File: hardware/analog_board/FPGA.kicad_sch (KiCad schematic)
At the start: 0 parts

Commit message: 1、FPGA最小系统原理图 2、DAC电路原理图 3、FPGA DAC 预布局
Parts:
- added R21: 100R, Resistor_SMD:R_0402_1005Metric, symbol Device:R
- added RN2, RN3, RN4, RN5, RN6, RN7, RN8, RN9: 33R, Resistor_SMD:R_Array_Concave_4x0402, symbol Device:R_Pack04
- added U1: GW2A-LV18EQ144, ArbWave30_lib:QFP-144_20x20_Pitch0.5mm, symbol ArbWave30_lib:GW2AR-LV18EQ144C8/I7
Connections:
- new net: RN7.5 (R4.2), U1.64 (IOB40A)
- new net: RN7.6 (R3.2), U1.63 (IOB38B)
- new net: RN7.7 (R2.2), U1.62 (IOB38A)
- new net: RN7.8 (R1.2), U1.61 (IOB34B)
- new net: RN3.5 (R4.2), U1.49 (IOB17B)
- new net: RN3.6 (R3.2), U1.48 (IOB17A)
- new net: RN3.7 (R2.2), U1.47 (IOB14B)
- new net: RN3.8 (R1.2), U1.46 (IOB14A)
- new net: RN2.5 (R4.2), U1.54 (IOB22B)
- new net: RN2.6 (R3.2), U1.52 (IOB22A)
- new net: RN2.7 (R2.2), U1.51 (IOB20B)
- new net: RN2.8 (R1.2), U1.50 (IOB20A)
- new net: RN9.5 (R4.2), U1.72 (IOB55B)
- new net: RN9.6 (R3.2), U1.71 (IOB53B)
- new net: RN9.7 (R2.2), U1.70 (IOB53A)
- new net: RN9.8 (R1.2), U1.69 (IOB48B)
- new net: RN5.8 (R1.2), U1.38 (IOB5A)
- new net: RN5.7 (R2.2), U1.39 (IOB5B)
- new net: RN5.6 (R3.2), U1.40 (IOB6A)
- new net: RN5.5 (R4.2), U1.41 (IOB6B)
- new net: RN4.8 (R1.2), U1.42 (IOB7A)
- new net: RN4.7 (R2.2), U1.43 (IOB7B)
- new net: RN4.6 (R3.2), U1.44 (IOB12A)
- new net: RN4.5 (R4.2), U1.45 (IOB12B)
- new net: RN8.5 (R4.2), U1.68 (IOB48A)
- new net: RN8.6 (R3.2), U1.67 (IOB42B)
- new net: RN8.7 (R2.2), U1.66 (IOB42A)
- new net: RN8.8 (R1.2), U1.65 (IOB40B)
- new net: RN6.8 (R1.2), U1.57 (IOB30B/GCLKC_4)
- new net: RN6.7 (R2.2), U1.58 (IOB33A)
- new net: RN6.6 (R3.2), U1.59 (IOB33B)
- new net: RN6.5 (R4.2), U1.60 (IOB34A)
- new net +3.3V: U1.103 (VCCX/VCC_IO2/VCC_IO6/VCC_IO7), U1.109 (VCC_IO1), U1.127 (VCC_IO0), U1.19 (VCCX/VCC_IO2/VCC_IO6/VCC_IO7), U1.31 (VCCX/VCC_IO2/VCC_IO6/VCC_IO7), U1.37 (VCC_IO5), U1.5 (VCCX/VCC_IO2/VCC_IO6/VCC_IO7), U1.55 (VCC_IO4), U1.77 (VCC_IO3), U1.91 (VCC_IO3)
- new net Ctrl_FPGA_NRST: U1.128 (IOT19A)
- new net Ctrl_SPI_CLK: U1.131 (IOT14B)
- new net Ctrl_SPI_CS: U1.132 (IOT14A)
- new net Ctrl_SPI_MISO: U1.130 (IOT17A)
- new net Ctrl_SPI_MOSI: U1.129 (IOT17B)
- new net DAC_SPI.DAC_SPI_CLK: U1.33 (IOL42B)
- new net DAC_SPI.DAC_SPI_CS: U1.32 (IOL42A)
- new net DAC_SPI.DAC_SPI_MISO: U1.35 (IOL45B/LPLL2_C_in)
- new net DAC_SPI.DAC_SPI_MOSI: U1.34 (IOL45A/LPLL2_T_in)
- new net Data_Clock: U1.56 (IOB30A/GCLKT_4)
- new net FPGA_CLK+: R21.2, U1.106 (IOR7A/RPLL1_T_in)
- new net FPGA_CLK-: R21.1, U1.105 (IOR7B/RPLL1_C_in)
- new net GND: U1.107 (VSS), U1.145 (EPAD), U1.17 (VSS), U1.2 (VSS), U1.53 (VSS), U1.74 (VSS), U1.89 (VSS)
- new net P1D0: RN6.1 (R1.1)
- new net P1D1: RN6.2 (R2.1)
- new net P1D10: RN8.3 (R3.1)
- new net P1D11: RN8.4 (R4.1)
- new net P1D12: RN9.1 (R1.1)
- new net P1D13: RN9.2 (R2.1)
- new net P1D14: RN9.3 (R3.1)
- new net P1D15: RN9.4 (R4.1)
- new net P1D2: RN6.3 (R3.1)
- new net P1D3: RN6.4 (R4.1)
- new net P1D4: RN7.1 (R1.1)
- new net P1D5: RN7.2 (R2.1)
- new net P1D6: RN7.3 (R3.1)
- new net P1D7: RN7.4 (R4.1)
- new net P1D8: RN8.1 (R1.1)
- new net P1D9: RN8.2 (R2.1)
- new net P2D0: RN5.1 (R1.1)
- new net P2D1: RN5.2 (R2.1)
- new net P2D10: RN3.3 (R3.1)
- new net P2D11: RN3.4 (R4.1)
- new net P2D12: RN2.1 (R1.1)
- new net P2D13: RN2.2 (R2.1)
- new net P2D14: RN2.3 (R3.1)
- new net P2D15: RN2.4 (R4.1)
- new net P2D2: RN5.3 (R3.1)
- new net P2D3: RN5.4 (R4.1)
- new net P2D4: RN4.1 (R1.1)
- new net P2D5: RN4.2 (R2.1)
- new net P2D6: RN4.3 (R3.1)
- new net P2D7: RN4.4 (R4.1)
- new net P2D8: RN3.1 (R1.1)
- new net P2D9: RN3.2 (R2.1)
- new net VCC_Core: U1.1 (VCC/VCC_PLLL1), U1.108 (VCC/VCC_PLLL1), U1.36 (VCC/VCC_PLLL1), U1.73 (VCC/VCC_PLLL1)
- new net VCC_PLLL: U1.8 (VCCPLL_L0)
- new net VCC_PLLR: U1.104 (VCCPLL_R0), U1.81 (VCCPLL_R1)

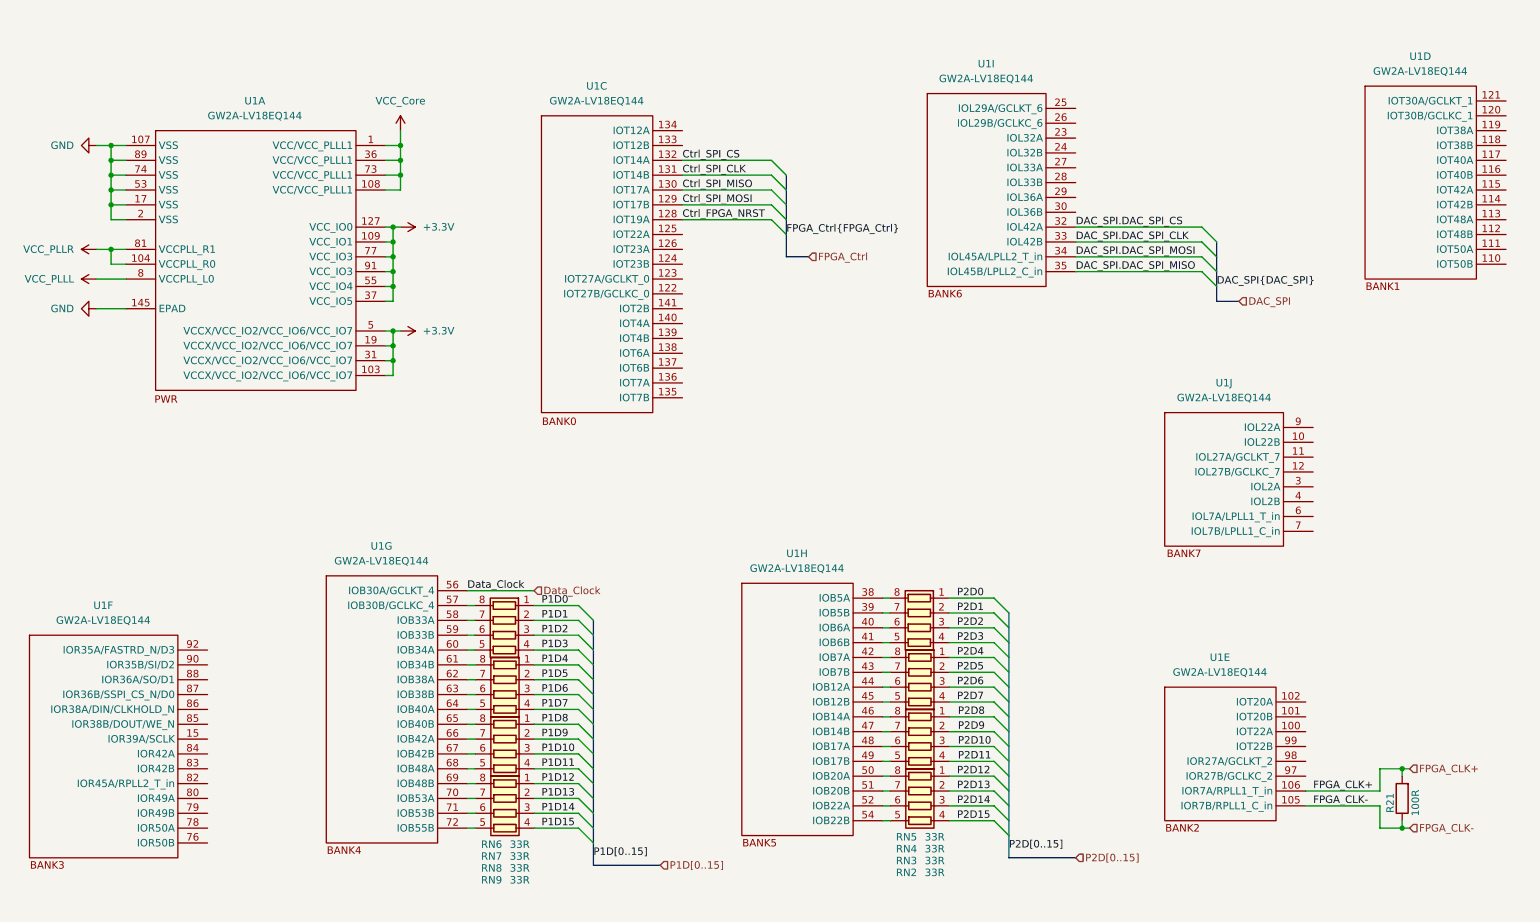
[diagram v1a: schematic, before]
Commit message: feat: 滤波器&差分转单端电路原理图
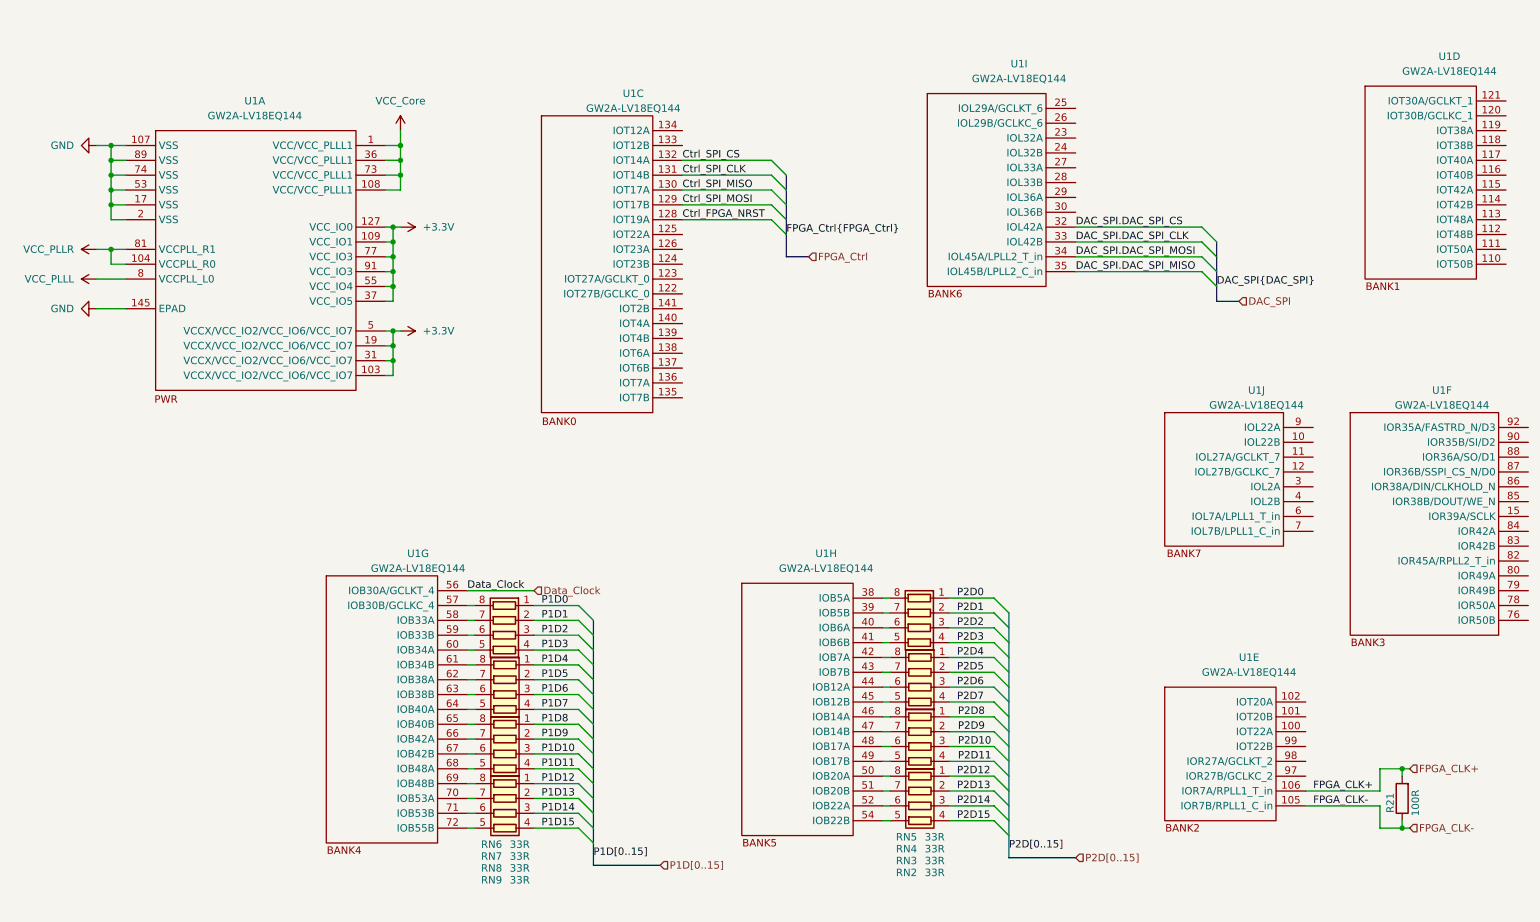
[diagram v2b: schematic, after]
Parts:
- U1: footprint ArbWave30_lib:QFP-144_20x20_Pitch0.5mm -> ArbWave30_lib:LQFP-144_20x20_Pitch0.5mm
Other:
- moved on the sheet: U1F
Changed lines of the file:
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@@
 		)
 	)
+	(rule_area
+		(exclude_from_sim no)
+		(in_bom yes)
+		(on_board yes)
+		(dnp no)
+		(polyline
+			(pts
+				(xy 172.085 110.49) (xy 172.72 157.48) (xy 189.23 157.48) (xy 188.595 110.49)
+			)
+			(stroke
+				(width 0)
+				(type dash)
+			)
+			(fill
+				(type none)
+			)
+		)
+	)
+	(rule_area
+		(exclude_from_sim no)
+		(in_bom yes)
+		(on_board yes)
+		(dnp no)
+		(polyline
+			(pts
+				(xy 100.965 109.22) (xy 101.6 156.21) (xy 118.11 156.21) (xy 117.475 109.22)
+			)
+			(stroke
+				(width 0)
+				(type dash)
+			)
+			(fill
+				(type none)
+			)
+		)
+	)
+	(netclass_flag ""
+		(length 2.54)
+		(shape round)
+		(at 104.14 109.22 0)
+		(fields_autoplaced yes)
+		(effects
+			(font
+				(size 1.27 1.27)
+			)
+			(justify left bottom)
+		)
+		(property "网络类" "DAC_data_port"
+			(at 104.8385 106.68 0)
+			(show_name no)
+			(do_not_autoplace no)
+			(effects
+				(font
+					(size 1.27 1.27)
+				)
+				(justify left)
+			)
+		)
+		(property "Component Class" ""
+			(at -39.37 -8.89 0)
+			(show_name no)
+			(do_not_autoplace no)
+			(effects
+				(font
+					(size 1.27 1.27)
+					(italic yes)
+				)
+			)
+		)
+	)
+	(netclass_flag ""
+		(length 2.54)
+		(shape round)
+		(at 175.26 110.49 0)
+		(fields_autoplaced yes)
+		(effects
+			(font
+				(size 1.27 1.27)
+			)
+			(justify left bottom)
+		)
+		(property "网络类" "DAC_data_port"
+			(at 175.9585 107.95 0)
+			(show_name no)
+			(do_not_autoplace no)
+			(effects
+				(font
+					(size 1.27 1.27)
+				)
+				(justify left)
+			)
+		)
+		(property "Component Class" ""
+			(at 31.75 -7.62 0)
+			(show_name no)
+			(do_not_autoplace no)
+			(effects
+				(font
+					(size 1.27 1.27)
+					(italic yes)
+				)
+			)
+		)
+	)
 	(symbol
 		(lib_id "Device:R")
@@
 		(fields_autoplaced yes)
 		(property "Reference" "U1"
-			(at 230.4312 124.46 0)
+			(at 235.4205 124.46 0)
 			(show_name no)
 			(do_not_autoplace no)
@@
 		)
 		(property "Value" "GW2A-LV18EQ144"
-			(at 230.4312 127 0)
+			(at 235.4205 127 0)
 			(show_name no)
 			(do_not_autoplace no)
@@
 			)
 		)
-		(property "Footprint" "ArbWave30_lib:QFP-144_20x20_Pitch0.5mm"
+		(property "Footprint" "ArbWave30_lib:LQFP-144_20x20_Pitch0.5mm"
 			(at 229.616 122.682 0)
 			(hide yes)
@@
 		(fields_autoplaced yes)
 		(property "Reference" "U1"
-			(at 264.7212 21.59 0)
+			(at 269.7105 21.59 0)
 			(show_name no)
 			(do_not_autoplace no)
@@
 		)
 		(property "Value" "GW2A-LV18EQ144"
-			(at 264.7212 24.13 0)
+			(at 269.7105 24.13 0)
 			(show_name no)
 			(do_not_autoplace no)
@@
 			)
 		)
-		(property "Footprint" "ArbWave30_lib:QFP-144_20x20_Pitch0.5mm"
+		(property "Footprint" "ArbWave30_lib:LQFP-144_20x20_Pitch0.5mm"
 			(at 263.906 19.812 0)
 			(hide yes)
@@
 		(fields_autoplaced yes)
 		(property "Reference" "U1"
-			(at 158.0412 106.68 0)
+			(at 163.0305 106.68 0)
 			(show_name no)
 			(do_not_autoplace no)
@@
 		)
 		(property "Value" "GW2A-LV18EQ144"
-			(at 158.0412 109.22 0)
+			(at 163.0305 109.22 0)
 			(show_name no)
 			(do_not_autoplace no)
@@
 			)
 		)
-		(property "Footprint" "ArbWave30_lib:QFP-144_20x20_Pitch0.5mm"
+		(property "Footprint" "ArbWave30_lib:LQFP-144_20x20_Pitch0.5mm"
 			(at 157.226 104.902 0)
 			(hide yes)
@@
 	(symbol
 		(lib_id "ArbWave30_lib:GW2AR-LV18EQ144C8/I7")
-		(at 24.13 118.11 0)
+		(at 250.19 80.01 0)
 		(unit 6)
 		(body_style 1)
@@
 		(fields_autoplaced yes)
 		(property "Reference" "U1"
-			(at 39.2962 115.57 0)
+			(at 268.4405 78.74 0)
 			(show_name no)
 			(do_not_autoplace no)
@@
 		)
 		(property "Value" "GW2A-LV18EQ144"
-			(at 39.2962 118.11 0)
+			(at 268.4405 81.28 0)
 			(show_name no)
 			(do_not_autoplace no)
@@
 			)
 		)
-		(property "Footprint" "ArbWave30_lib:QFP-144_20x20_Pitch0.5mm"
-			(at 36.576 115.062 0)
+		(property "Footprint" "ArbWave30_lib:LQFP-144_20x20_Pitch0.5mm"
+			(at 262.636 76.962 0)
 			(hide yes)
 			(show_name no)
@@
 		)
 		(property "Datasheet" ""
-			(at 24.13 118.11 0)
+			(at 250.19 80.01 0)
 			(hide yes)
 			(show_name no)
@@
 		)
 		(property "Description" ""
-			(at 24.13 118.11 0)
+			(at 250.19 80.01 0)
 			(hide yes)
 			(show_name no)
@@
 		(fields_autoplaced yes)
 		(property "Reference" "U1"
-			(at 86.9212 105.41 0)
+			(at 93.1805 106.68 0)
 			(show_name no)
 			(do_not_autoplace no)
@@
 		)
 		(property "Value" "GW2A-LV18EQ144"
-			(at 86.9212 107.95 0)
+			(at 93.1805 109.22 0)
 			(show_name no)
 			(do_not_autoplace no)
@@
 			)
 		)
-		(property "Footprint" "ArbWave30_lib:QFP-144_20x20_Pitch0.5mm"
+		(property "Footprint" "ArbWave30_lib:LQFP-144_20x20_Pitch0.5mm"
 			(at 87.376 104.902 0)
 			(hide yes)
@@
 		(fields_autoplaced yes)
 		(property "Reference" "U1"
-			(at 123.7512 26.67 0)
+			(at 130.0105 27.94 0)
 			(show_name no)
 			(do_not_autoplace no)
@@
 		)
 		(property "Value" "GW2A-LV18EQ144"
-			(at 123.7512 29.21 0)
+			(at 130.0105 30.48 0)
 			(show_name no)
 			(do_not_autoplace no)
@@
 			)
 		)
-		(property "Footprint" "ArbWave30_lib:QFP-144_20x20_Pitch0.5mm"
+		(property "Footprint" "ArbWave30_lib:LQFP-144_20x20_Pitch0.5mm"
 			(at 124.206 26.162 0)
 			(hide yes)
@@
 		(fields_autoplaced yes)
 		(property "Reference" "U1"
-			(at 190.4262 22.86 0)
+			(at 196.0505 22.86 0)
 			(show_name no)
 			(do_not_autoplace no)
@@
 		)
 		(property "Value" "GW2A-LV18EQ144"
-			(at 190.4262 25.4 0)
+			(at 196.0505 25.4 0)
 			(show_name no)
 			(do_not_autoplace no)
@@
 			)
 		)
-		(property "Footprint" "ArbWave30_lib:QFP-144_20x20_Pitch0.5mm"
+		(property "Footprint" "ArbWave30_lib:LQFP-144_20x20_Pitch0.5mm"
 			(at 190.246 21.082 0)
 			(hide yes)
@@
 		(fields_autoplaced yes)
 		(property "Reference" "U1"
-			(at 231.14 77.47 0)
+			(at 236.6905 78.74 0)
 			(show_name no)
 			(do_not_autoplace no)
@@
 		)
 		(property "Value" "GW2A-LV18EQ144"
-			(at 231.14 80.01 0)
+			(at 236.6905 81.28 0)
 			(show_name no)
 			(do_not_autoplace no)
@@
 			)
 		)
-		(property "Footprint" "ArbWave30_lib:QFP-144_20x20_Pitch0.5mm"
+		(property "Footprint" "ArbWave30_lib:LQFP-144_20x20_Pitch0.5mm"
 			(at 230.886 76.962 0)
 			(hide yes)
@@
 			)
 		)
-		(property "Footprint" "ArbWave30_lib:QFP-144_20x20_Pitch0.5mm"
+		(property "Footprint" "ArbWave30_lib:LQFP-144_20x20_Pitch0.5mm"
 			(at 59.436 27.432 0)
 			(hide yes)

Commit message: feat：时钟电路原理图
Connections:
- net Clock_NRST: now reaches U1.110 (IOT50B)
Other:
- moved on the sheet: R21, RN2, RN3, RN4, RN5, RN6, RN7, RN8, RN9, U1D, U1E, U1F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

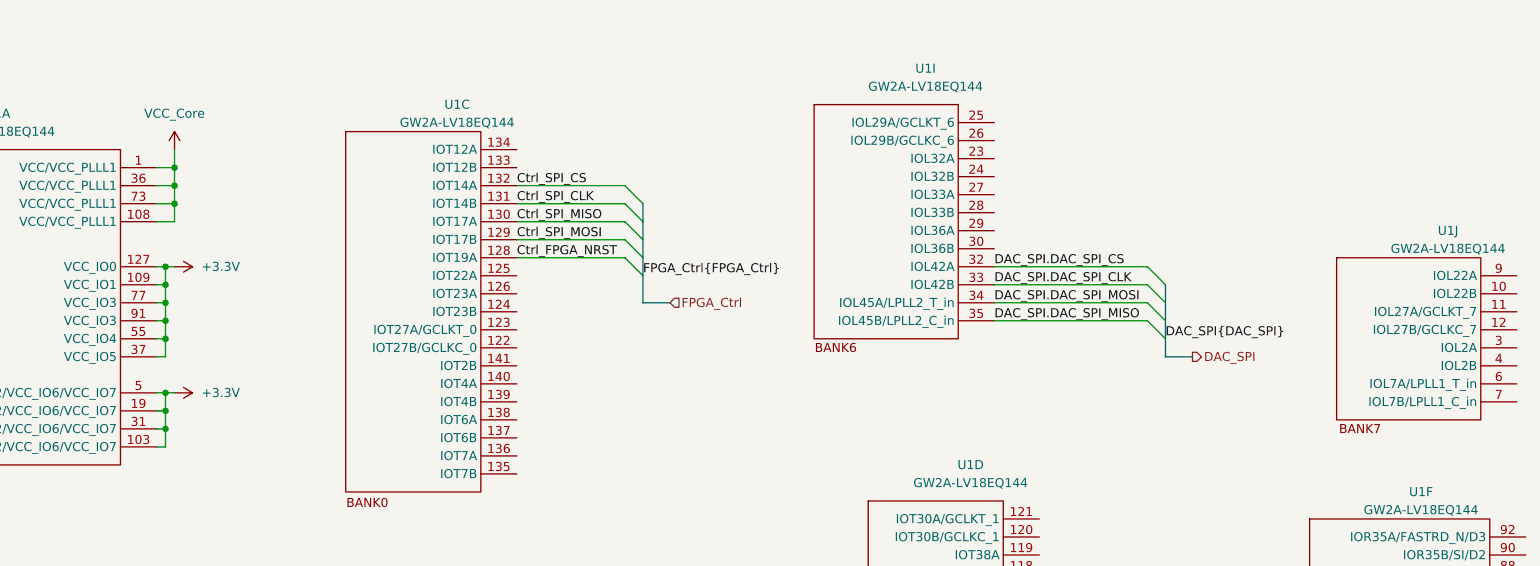
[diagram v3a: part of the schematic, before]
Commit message: feat：完成模拟板板间接口设计
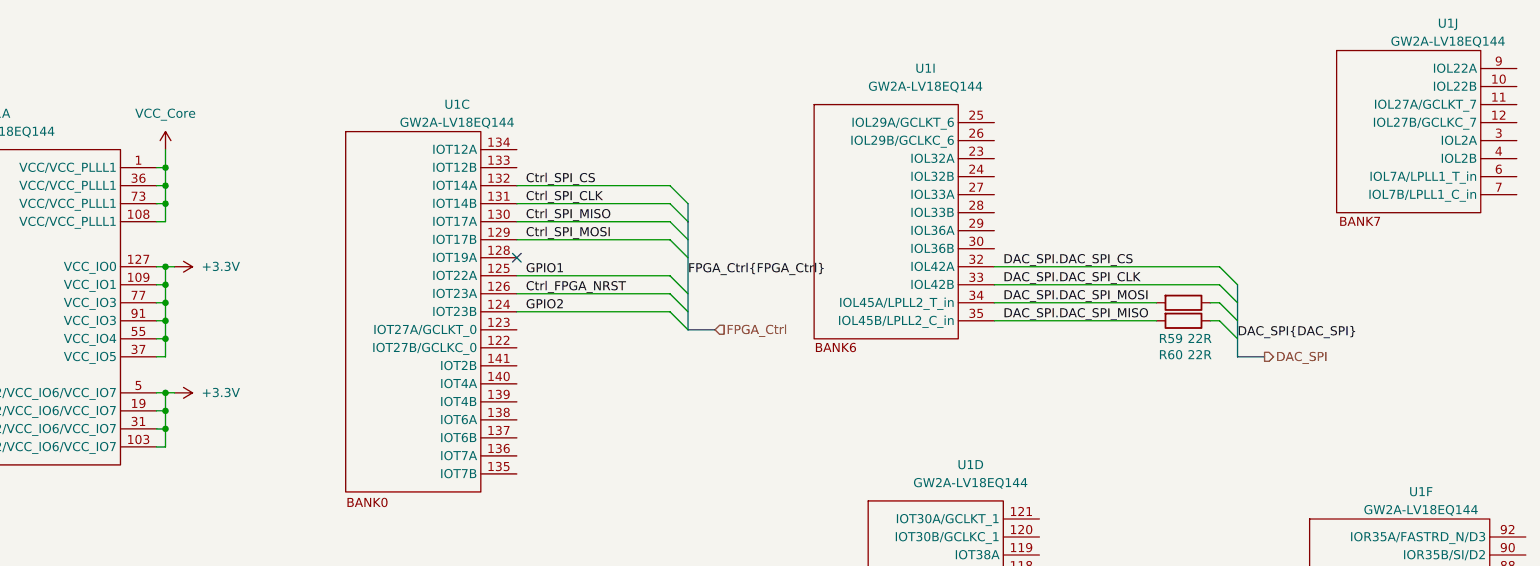
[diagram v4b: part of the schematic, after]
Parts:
- added R59, R60: 22R, Resistor_SMD:R_0402_1005Metric, symbol Device:R
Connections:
- net Ctrl_FPGA_NRST: now also U1.126 (IOT23A); no longer U1.128 (IOT19A)
- net DAC_SPI.DAC_SPI_MISO: now also R60.2
- net DAC_SPI.DAC_SPI_MOSI: now also R59.2
- net GPIO2: now reaches U1.124 (IOT23B)
- net GPIO1: now reaches U1.125 (IOT22A)
- no-connect marks 0 -> 1
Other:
- moved on the sheet: U1J
